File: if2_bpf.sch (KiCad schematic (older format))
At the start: 12 parts

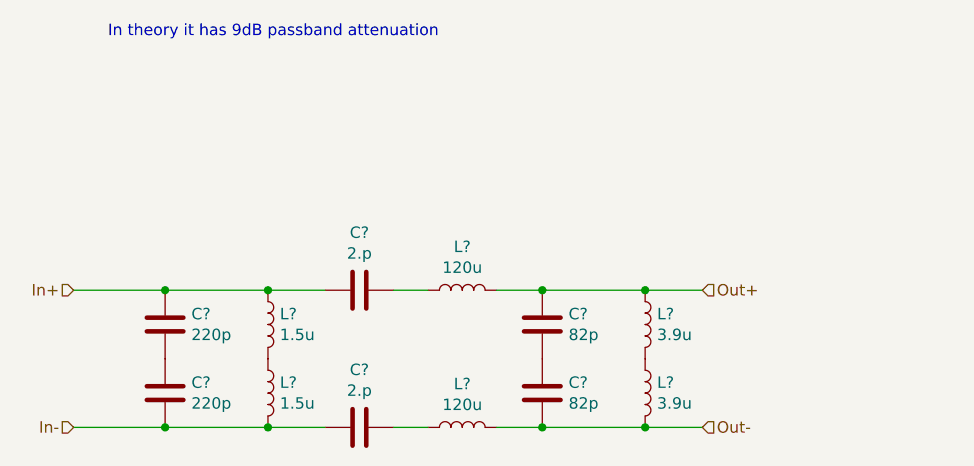
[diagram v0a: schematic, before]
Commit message: If2 50 ohm filter
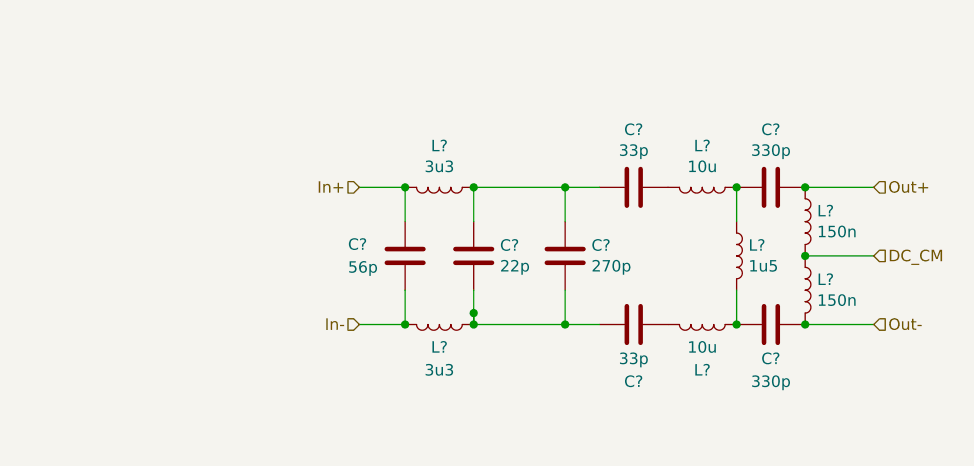
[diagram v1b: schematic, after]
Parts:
- removed C? (x2): 220p, symbol Device:C
- removed C? (x2): 2.p, symbol Device:C
- removed C? (x2): 82p, symbol Device:C
- removed L? (x2): 1.5u, symbol Device:L
- removed L? (x2): 120u, symbol Device:L
- removed L? (x2): 3.9u, symbol Device:L
- added C?: 56p, symbol Device:C
- added C?: 22p, symbol Device:C
- added C? (x2): 33p, symbol Device:C
- added C? (x2): 330p, symbol Device:C
- added C?: 270p, symbol Device:C
- added L? (x2): 3u3, symbol Device:L
- added L? (x2): 10u, symbol Device:L
- added L?: 1u5, symbol Device:L
- added L? (x2): 150n, symbol Device:L
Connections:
- net In+: now also C?.1, L?.2
- net In-: now also C?.2, L?.2
- net Out+: now also C?.1, L?.1
- net Out-: now also C?.2, L?.2
- new net: C?.1, C?.1, C?.2, L?.1
- new net: C?.2, C?.2, C?.2, L?.1
- new net: C?.1, L?.2 (x2)
- new net: C?.2, L?.1, L?.1
- new net: C?.1, L?.1, L?.2
- new net DC_CM: L?.1, L?.2
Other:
- note removed: "In theory it has 9dB passband attenuation\n"

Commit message: Initalize receiver test circuit
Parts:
- gave numbers to parts that had none: 14
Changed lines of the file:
@@
 $Descr A4 11693 8268
 encoding utf-8
-Sheet 5 9
+Sheet 5 7
 Title ""
 Date ""
@@
 In-
 $Comp
-L Device:C C?
+L Device:C C24
 U 1 1 5FECCD6C
 P 4750 2300
-F 0 "C?" H 4500 2350 50  0000 L CNN
+F 0 "C24" H 4500 2350 50  0000 L CNN
 F 1 "56p" H 4500 2250 50  0000 L CNN
 F 2 "" H 4788 2150 50  0001 C CNN
@@
 $EndComp
 $Comp
-L Device:L L?
+L Device:L L11
 U 1 1 5FECD51B
 P 4900 2000
-F 0 "L?" V 4719 2000 50  0000 C CNN
+F 0 "L11" V 4719 2000 50  0000 C CNN
 F 1 "3u3" V 4810 2000 50  0000 C CNN
 F 2 "" H 4900 2000 50  0001 C CNN
@@
 $EndComp
 $Comp
-L Device:L L?
+L Device:L L12
 U 1 1 5FECDA86
 P 4900 2600
-F 0 "L?" V 5000 2600 50  0000 C CNN
+F 0 "L12" V 5000 2600 50  0000 C CNN
 F 1 "3u3" V 5100 2600 50  0000 C CNN
 F 2 "" H 4900 2600 50  0001 C CNN
@@
 $EndComp
 $Comp
-L Device:C C?
+L Device:C C25
 U 1 1 5FECE707
 P 5050 2300
-F 0 "C?" H 5165 2346 50  0000 L CNN
+F 0 "C25" H 5165 2346 50  0000 L CNN
 F 1 "22p" H 5165 2255 50  0000 L CNN
 F 2 "" H 5088 2150 50  0001 C CNN
@@
 $EndComp
 $Comp
-L Device:C C?
+L Device:C C27
 U 1 1 5FECF0CE
 P 5750 2000
-F 0 "C?" V 5498 2000 50  0000 C CNN
+F 0 "C27" V 5498 2000 50  0000 C CNN
 F 1 "33p" V 5589 2000 50  0000 C CNN
 F 2 "" H 5788 1850 50  0001 C CNN
@@
 $EndComp
 $Comp
-L Device:L L?
+L Device:L L13
 U 1 1 5FECF5C4
 P 6050 2000
-F 0 "L?" V 5869 2000 50  0000 C CNN
+F 0 "L13" V 5869 2000 50  0000 C CNN
 F 1 "10u" V 5960 2000 50  0000 C CNN
 F 2 "" H 6050 2000 50  0001 C CNN
@@
 $EndComp
 $Comp
-L Device:L L?
+L Device:L L15
 U 1 1 5FED0166
 P 6200 2300
-F 0 "L?" H 6252 2346 50  0000 L CNN
+F 0 "L15" H 6252 2346 50  0000 L CNN
 F 1 "1u5" H 6252 2255 50  0000 L CNN
 F 2 "" H 6200 2300 50  0001 C CNN
@@
 $EndComp
 $Comp
-L Device:C C?
+L Device:C C29
 U 1 1 5FED1E6D
 P 6350 2000
-F 0 "C?" V 6098 2000 50  0000 C CNN
+F 0 "C29" V 6098 2000 50  0000 C CNN
 F 1 "330p" V 6189 2000 50  0000 C CNN
 F 2 "" H 6388 1850 50  0001 C CNN
@@
 $EndComp
 $Comp
-L Device:L L?
+L Device:L L16
 U 1 1 5FED258A
 P 6500 2150
-F 0 "L?" H 6552 2196 50  0000 L CNN
+F 0 "L16" H 6552 2196 50  0000 L CNN
 F 1 "150n" H 6552 2105 50  0000 L CNN
 F 2 "" H 6500 2150 50  0001 C CNN
@@
 $EndComp
 $Comp
-L Device:L L?
+L Device:L L17
 U 1 1 5FED3759
 P 6500 2450
-F 0 "L?" H 6552 2496 50  0000 L CNN
+F 0 "L17" H 6552 2496 50  0000 L CNN
 F 1 "150n" H 6552 2405 50  0000 L CNN
 F 2 "" H 6500 2450 50  0001 C CNN
@@
 DC_CM
 $Comp
-L Device:C C?
+L Device:C C30
 U 1 1 5FED6CF7
 P 6350 2600
-F 0 "C?" V 6200 2600 50  0000 C CNN
+F 0 "C30" V 6200 2600 50  0000 C CNN
 F 1 "330p" V 6100 2600 50  0000 C CNN
 F 2 "" H 6388 2450 50  0001 C CNN
@@
 Connection ~ 6500 2600
 $Comp
-L Device:L L?
+L Device:L L14
 U 1 1 5FED7875
 P 6050 2600
-F 0 "L?" V 6250 2600 50  0000 C CNN
+F 0 "L14" V 6250 2600 50  0000 C CNN
 F 1 "10u" V 6150 2600 50  0000 C CNN
 F 2 "" H 6050 2600 50  0001 C CNN
@@
 $EndComp
 $Comp
-L Device:C C?
+L Device:C C28
 U 1 1 5FED7DBE
 P 5750 2600
-F 0 "C?" V 6000 2600 50  0000 C CNN
+F 0 "C28" V 6000 2600 50  0000 C CNN
 F 1 "33p" V 5900 2600 50  0000 C CNN
 F 2 "" H 5788 2450 50  0001 C CNN
@@
 Connection ~ 6200 2600
 $Comp
-L Device:C C?
+L Device:C C26
 U 1 1 5FEE51AD
 P 5450 2300
-F 0 "C?" H 5565 2346 50  0000 L CNN
+F 0 "C26" H 5565 2346 50  0000 L CNN
 F 1 "270p" H 5565 2255 50  0000 L CNN
 F 2 "" H 5488 2150 50  0001 C CNN

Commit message: Nyáktervezésre majdnem kész
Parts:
- C24, C25, C26, C27, C28, C29, C30: footprint (none) -> Capacitor_SMD:C_0805_2012Metric_Pad1.15x1.40mm_HandSolder
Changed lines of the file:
@@
 F 0 "C24" H 4500 2350 50  0000 L CNN
 F 1 "56p" H 4500 2250 50  0000 L CNN
-F 2 "" H 4788 2150 50  0001 C CNN
+F 2 "Capacitor_SMD:C_0805_2012Metric_Pad1.15x1.40mm_HandSolder" H 4788 2150 50  0001 C CNN
 F 3 "~" H 4750 2300 50  0001 C CNN
 	1    4750 2300
@@
 F 0 "C25" H 5165 2346 50  0000 L CNN
 F 1 "22p" H 5165 2255 50  0000 L CNN
-F 2 "" H 5088 2150 50  0001 C CNN
+F 2 "Capacitor_SMD:C_0805_2012Metric_Pad1.15x1.40mm_HandSolder" H 5088 2150 50  0001 C CNN
 F 3 "~" H 5050 2300 50  0001 C CNN
 	1    5050 2300
@@
 F 0 "C27" V 5498 2000 50  0000 C CNN
 F 1 "33p" V 5589 2000 50  0000 C CNN
-F 2 "" H 5788 1850 50  0001 C CNN
+F 2 "Capacitor_SMD:C_0805_2012Metric_Pad1.15x1.40mm_HandSolder" H 5788 1850 50  0001 C CNN
 F 3 "~" H 5750 2000 50  0001 C CNN
 	1    5750 2000
@@
 F 0 "C29" V 6098 2000 50  0000 C CNN
 F 1 "330p" V 6189 2000 50  0000 C CNN
-F 2 "" H 6388 1850 50  0001 C CNN
+F 2 "Capacitor_SMD:C_0805_2012Metric_Pad1.15x1.40mm_HandSolder" H 6388 1850 50  0001 C CNN
 F 3 "~" H 6350 2000 50  0001 C CNN
 	1    6350 2000
@@
 F 0 "C30" V 6200 2600 50  0000 C CNN
 F 1 "330p" V 6100 2600 50  0000 C CNN
-F 2 "" H 6388 2450 50  0001 C CNN
+F 2 "Capacitor_SMD:C_0805_2012Metric_Pad1.15x1.40mm_HandSolder" H 6388 2450 50  0001 C CNN
 F 3 "~" H 6350 2600 50  0001 C CNN
 	1    6350 2600
@@
 F 0 "C28" V 6000 2600 50  0000 C CNN
 F 1 "33p" V 5900 2600 50  0000 C CNN
-F 2 "" H 5788 2450 50  0001 C CNN
+F 2 "Capacitor_SMD:C_0805_2012Metric_Pad1.15x1.40mm_HandSolder" H 5788 2450 50  0001 C CNN
 F 3 "~" H 5750 2600 50  0001 C CNN
 	1    5750 2600
@@
 F 0 "C26" H 5565 2346 50  0000 L CNN
 F 1 "270p" H 5565 2255 50  0000 L CNN
-F 2 "" H 5488 2150 50  0001 C CNN
+F 2 "Capacitor_SMD:C_0805_2012Metric_Pad1.15x1.40mm_HandSolder" H 5488 2150 50  0001 C CNN
 F 3 "~" H 5450 2300 50  0001 C CNN
 	1    5450 2300
@@
 Wire Wire Line
 	5450 2000 5050 2000
-Connection ~ 5050 2550
 Wire Wire Line
 	5050 2550 5050 2600

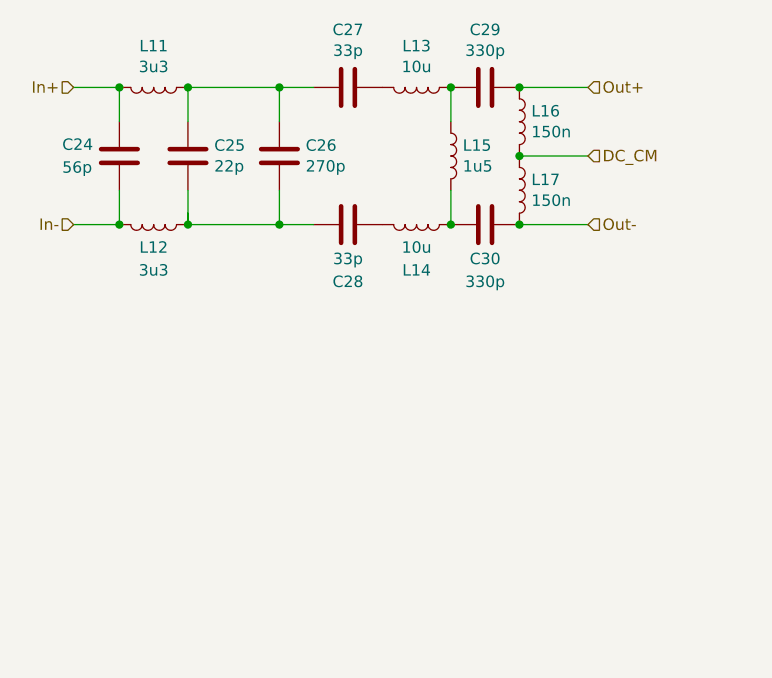
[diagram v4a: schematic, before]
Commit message: Receiver test panel ++
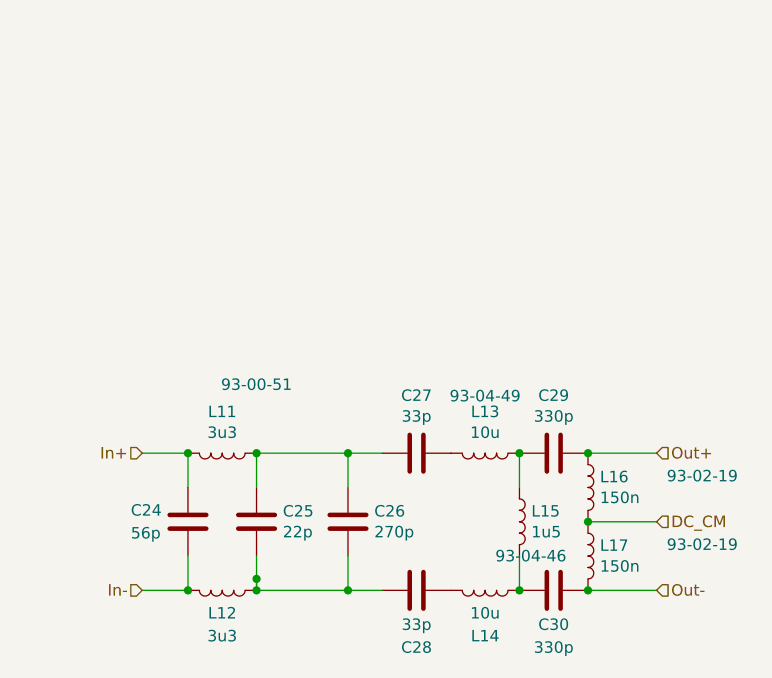
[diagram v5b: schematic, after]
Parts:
- L11: footprint (none) -> Inductor_SMD:L_1210_3225Metric_Pad1.42x2.65mm_HandSolder; Lomex (none) -> 93-00-51
- L12, L14: footprint (none) -> Inductor_SMD:L_1210_3225Metric_Pad1.42x2.65mm_HandSolder
- L13: footprint (none) -> Inductor_SMD:L_1210_3225Metric_Pad1.42x2.65mm_HandSolder; Lomex (none) -> 93-04-49
- L15: footprint (none) -> Inductor_SMD:L_1210_3225Metric_Pad1.42x2.65mm_HandSolder; Lomex (none) -> 93-04-46
- L16, L17: footprint (none) -> Inductor_SMD:L_1210_3225Metric_Pad1.42x2.65mm_HandSolder; Lomex (none) -> 93-02-19
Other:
- moved on the sheet: C24, C25, C26, C27, C28, C29, C30, L11, L12, L13, L14, L15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

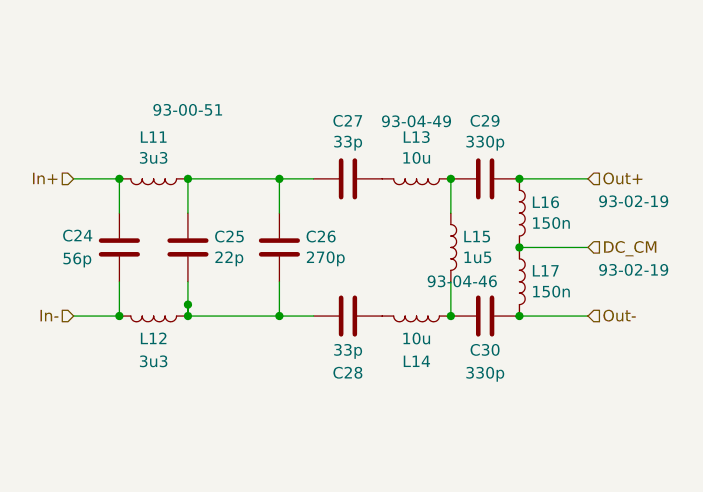
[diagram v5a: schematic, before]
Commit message: IF2 filter and amp recalculate
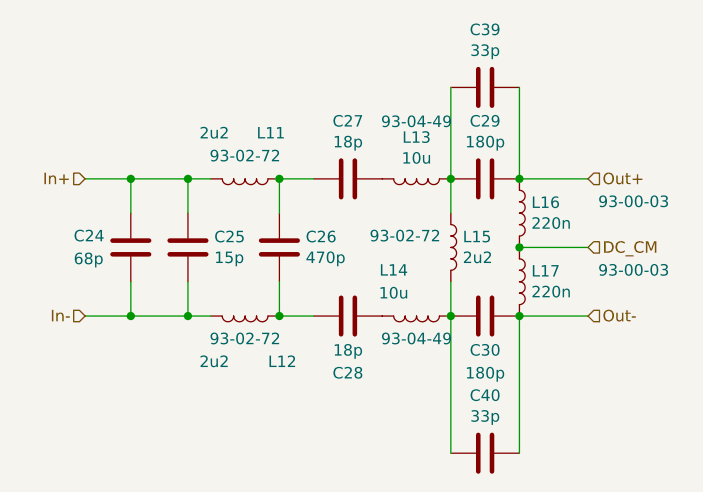
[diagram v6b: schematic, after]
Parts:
- added C39, C40: 33p, Capacitor_SMD:C_0805_2012Metric_Pad1.15x1.40mm_HandSolder, symbol Device:C
- C24: value 56p -> 68p
- C25: value 22p -> 15p
- C26: value 270p -> 470p
- C27, C28: value 33p -> 18p
- C29, C30: value 330p -> 180p
- L11: value 3u3 -> 2u2; footprint Inductor_SMD:L_1210_3225Metric_Pad1.42x2.65mm_HandSolder -> Inductor_SMD:L_0805_2012Metric_Pad1.15x1.40mm_HandSolder; Lomex 93-00-51 -> 93-02-72
- L12: value 3u3 -> 2u2; footprint Inductor_SMD:L_1210_3225Metric_Pad1.42x2.65mm_HandSolder -> Inductor_SMD:L_0805_2012Metric_Pad1.15x1.40mm_HandSolder; Lomex (none) -> 93-02-72
- L14: Lomex (none) -> 93-04-49
- L15: value 1u5 -> 2u2; footprint Inductor_SMD:L_1210_3225Metric_Pad1.42x2.65mm_HandSolder -> Inductor_SMD:L_0805_2012Metric_Pad1.15x1.40mm_HandSolder; Lomex 93-04-46 -> 93-02-72
- L16, L17: value 150n -> 220n; Lomex 93-02-19 -> 93-00-03
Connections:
- net In+: now also C25.1
- net In-: now also C25.2
- net Out+: now also C39.1
- net Out-: now also C40.1
- net at C26.1, C27.2, L11.1: no longer C25.1
- net at C26.2, C28.2, L12.1: no longer C25.2
- net at C29.2, L13.1, L15.1: now also C39.2
- net at C30.1, L14.1, L15.2: now also C40.2
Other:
- moved on the sheet: C24
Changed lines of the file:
@@
 Text HLabel 7100 4200 2    50   Input ~ 0
 Out-
-Text HLabel 4850 3600 0    50   Input ~ 0
+Text HLabel 4900 3600 0    50   Input ~ 0
 In+
-Text HLabel 4850 4200 0    50   Input ~ 0
+Text HLabel 4900 4200 0    50   Input ~ 0
 In-
 $Comp
 L Device:C C24
 U 1 1 5FECCD6C
-P 5050 3900
-F 0 "C24" H 4800 3950 50  0000 L CNN
-F 1 "56p" H 4800 3850 50  0000 L CNN
-F 2 "Capacitor_SMD:C_0805_2012Metric_Pad1.15x1.40mm_HandSolder" H 5088 3750 50  0001 C CNN
-F 3 "~" H 5050 3900 50  0001 C CNN
-	1    5050 3900
-	1    0    0    -1
-$EndComp
-$Comp
-L Device:L L11
-U 1 1 5FECD51B
-P 5200 3600
-F 0 "L11" V 5019 3600 50  0000 C CNN
-F 1 "3u3" V 5110 3600 50  0000 C CNN
-F 2 "Inductor_SMD:L_1210_3225Metric_Pad1.42x2.65mm_HandSolder" H 5200 3600 50  0001 C CNN
-F 3 "~" H 5200 3600 50  0001 C CNN
-F 4 "93-00-51" V 4900 3750 50  0000 C CNN "Lomex"
-	1    5200 3600
-	0    1    1    0
-$EndComp
-$Comp
-L Device:L L12
-U 1 1 5FECDA86
-P 5200 4200
-F 0 "L12" V 5300 4200 50  0000 C CNN
-F 1 "3u3" V 5400 4200 50  0000 C CNN
-F 2 "Inductor_SMD:L_1210_3225Metric_Pad1.42x2.65mm_HandSolder" H 5200 4200 50  0001 C CNN
-F 3 "~" H 5200 4200 50  0001 C CNN
-	1    5200 4200
-	0    1    1    0
+P 5100 3900
+F 0 "C24" H 4850 3950 50  0000 L CNN
+F 1 "68p" H 4850 3850 50  0000 L CNN
+F 2 "Capacitor_SMD:C_0805_2012Metric_Pad1.15x1.40mm_HandSolder" H 5138 3750 50  0001 C CNN
+F 3 "~" H 5100 3900 50  0001 C CNN
+	1    5100 3900
+	1    0    0    -1
 $EndComp
 $Comp
@@
 P 5350 3900
 F 0 "C25" H 5465 3946 50  0000 L CNN
-F 1 "22p" H 5465 3855 50  0000 L CNN
+F 1 "15p" H 5465 3855 50  0000 L CNN
 F 2 "Capacitor_SMD:C_0805_2012Metric_Pad1.15x1.40mm_HandSolder" H 5388 3750 50  0001 C CNN
 F 3 "~" H 5350 3900 50  0001 C CNN
@@
 P 6050 3600
 F 0 "C27" V 5798 3600 50  0000 C CNN
-F 1 "33p" V 5889 3600 50  0000 C CNN
+F 1 "18p" V 5889 3600 50  0000 C CNN
 F 2 "Capacitor_SMD:C_0805_2012Metric_Pad1.15x1.40mm_HandSolder" H 6088 3450 50  0001 C CNN
 F 3 "~" H 6050 3600 50  0001 C CNN
@@
 P 6500 3900
 F 0 "L15" H 6552 3946 50  0000 L CNN
-F 1 "1u5" H 6552 3855 50  0000 L CNN
-F 2 "Inductor_SMD:L_1210_3225Metric_Pad1.42x2.65mm_HandSolder" H 6500 3900 50  0001 C CNN
+F 1 "2u2" H 6552 3855 50  0000 L CNN
+F 2 "Inductor_SMD:L_0805_2012Metric_Pad1.15x1.40mm_HandSolder" H 6500 3900 50  0001 C CNN
 F 3 "~" H 6500 3900 50  0001 C CNN
-F 4 "93-04-46" H 6550 3750 50  0000 C CNN "Lomex"
+F 4 "93-02-72" H 6300 3950 50  0000 C CNN "Lomex"
 	1    6500 3900
 	1    0    0    -1
@@
 P 6650 3600
 F 0 "C29" V 6398 3600 50  0000 C CNN
-F 1 "330p" V 6489 3600 50  0000 C CNN
+F 1 "180p" V 6489 3600 50  0000 C CNN
 F 2 "Capacitor_SMD:C_0805_2012Metric_Pad1.15x1.40mm_HandSolder" H 6688 3450 50  0001 C CNN
 F 3 "~" H 6650 3600 50  0001 C CNN
@@
 P 6800 3750
 F 0 "L16" H 6852 3796 50  0000 L CNN
-F 1 "150n" H 6852 3705 50  0000 L CNN
+F 1 "220n" H 6852 3705 50  0000 L CNN
 F 2 "Inductor_SMD:L_1210_3225Metric_Pad1.42x2.65mm_HandSolder" H 6800 3750 50  0001 C CNN
 F 3 "~" H 6800 3750 50  0001 C CNN
-F 4 "93-02-19" H 7300 3800 50  0000 C CNN "Lomex"
+F 4 "93-00-03" H 7300 3800 50  0000 C CNN "Lomex"
 	1    6800 3750
 	1    0    0    -1
 $EndComp
-$Comp
-L Device:L L17
-U 1 1 5FED3759
-P 6800 4050
-F 0 "L17" H 6852 4096 50  0000 L CNN
-F 1 "150n" H 6852 4005 50  0000 L CNN
-F 2 "Inductor_SMD:L_1210_3225Metric_Pad1.42x2.65mm_HandSolder" H 6800 4050 50  0001 C CNN
-F 3 "~" H 6800 4050 50  0001 C CNN
-F 4 "93-02-19" H 7300 4100 50  0000 C CNN "Lomex"
-	1    6800 4050
-	1    0    0    -1
-$EndComp
-Wire Wire Line
-	4850 4200 5050 4200
-Wire Wire Line
-	5050 4200 5050 4050
-Connection ~ 5050 4200
-Wire Wire Line
-	5050 3750 5050 3600
-Wire Wire Line
-	5050 3600 4850 3600
-Connection ~ 5050 3600
-Wire Wire Line
-	5350 3750 5350 3600
+Wire Wire Line
+	4900 4200 5100 4200
+Wire Wire Line
+	5100 4200 5100 4050
+Wire Wire Line
+	5100 3750 5100 3600
+Wire Wire Line
+	5100 3600 4900 3600
 Wire Wire Line
 	6500 3750 6500 3600
@@
 Wire Wire Line
 	6800 3900 7100 3900
-Connection ~ 6800 3900
 Text HLabel 7100 3900 2    50   Input ~ 0
 DC_CM
@@
 P 6650 4200
 F 0 "C30" V 6500 4200 50  0000 C CNN
-F 1 "330p" V 6400 4200 50  0000 C CNN
+F 1 "180p" V 6400 4200 50  0000 C CNN
 F 2 "Capacitor_SMD:C_0805_2012Metric_Pad1.15x1.40mm_HandSolder" H 6688 4050 50  0001 C CNN
 F 3 "~" H 6650 4200 50  0001 C CNN
@@
 	0    -1   -1   0
 $EndComp
-Connection ~ 6800 4200
-$Comp
-L Device:L L14
-U 1 1 5FED7875
-P 6350 4200
-F 0 "L14" V 6550 4200 50  0000 C CNN
-F 1 "10u" V 6450 4200 50  0000 C CNN
-F 2 "Inductor_SMD:L_1210_3225Metric_Pad1.42x2.65mm_HandSolder" H 6350 4200 50  0001 C CNN
-F 3 "~" H 6350 4200 50  0001 C CNN
-	1    6350 4200
-	0    1    1    0
-$EndComp
 $Comp
 L Device:C C28
@@
 P 6050 4200
 F 0 "C28" V 6300 4200 50  0000 C CNN
-F 1 "33p" V 6200 4200 50  0000 C CNN
+F 1 "18p" V 6200 4200 50  0000 C CNN
 F 2 "Capacitor_SMD:C_0805_2012Metric_Pad1.15x1.40mm_HandSolder" H 6088 4050 50  0001 C CNN
 F 3 "~" H 6050 4200 50  0001 C CNN
@@
 Wire Wire Line
 	6500 4050 6500 4200
-Connection ~ 6500 4200
 $Comp
 L Device:C C26
@@
 P 5750 3900
 F 0 "C26" H 5865 3946 50  0000 L CNN
-F 1 "270p" H 5865 3855 50  0000 L CNN
+F 1 "470p" H 5865 3855 50  0000 L CNN
 F 2 "Capacitor_SMD:C_0805_2012Metric_Pad1.15x1.40mm_HandSolder" H 5788 3750 50  0001 C CNN
 F 3 "~" H 5750 3900 50  0001 C CNN
@@
 Wire Wire Line
 	5900 4200 5750 4200
+Wire Wire Line
+	5750 4050 5750 4200
+Wire Wire Line
+	5900 3600 5750 3600
+Wire Wire Line
+	5750 3750 5750 3600
+Wire Wire Line
+	5450 3600 5350 3600
+Connection ~ 5100 3600
+Wire Wire Line
+	5350 3750 5350 3600
+Connection ~ 5350 3600
+Wire Wire Line
+	5350 3600 5100 3600
+Wire Wire Line
+	5450 4200 5350 4200
+Connection ~ 5100 4200
+Wire Wire Line
+	5350 4050 5350 4200
 Connection ~ 5350 4200
 Wire Wire Line
-	5750 4050 5750 4200
+	5350 4200 5100 4200
+$Comp
+L Device:L L11
+U 1 1 60028C2F
+P 5600 3600
+F 0 "L11" V 5400 3650 50  0000 L CNN
+F 1 "2u2" V 5400 3400 50  0000 L CNN
+F 2 "Inductor_SMD:L_0805_2012Metric_Pad1.15x1.40mm_HandSolder" H 5600 3600 50  0001 C CNN
+F 3 "~" H 5600 3600 50  0001 C CNN
+F 4 "93-02-72" V 5500 3600 50  0000 C CNN "Lomex"
+	1    5600 3600
+	0    1    1    0
+$EndComp
+Connection ~ 5750 3600
+$Comp
+L Device:L L12
+U 1 1 6002A199
+P 5600 4200
+F 0 "L12" V 5800 4300 50  0000 L CNN
+F 1 "2u2" V 5800 4000 50  0000 L CNN
+F 2 "Inductor_SMD:L_0805_2012Metric_Pad1.15x1.40mm_HandSolder" H 5600 4200 50  0001 C CNN
+F 3 "~" H 5600 4200 50  0001 C CNN
+F 4 "93-02-72" V 5700 4200 50  0000 C CNN "Lomex"
+	1    5600 4200
+	0    1    1    0
+$EndComp
 Connection ~ 5750 4200
-Wire Wire Line
-	5750 4200 5350 4200
-Wire Wire Line
-	5900 3600 5750 3600
-Connection ~ 5350 3600
-Wire Wire Line
-	5750 3750 5750 3600
-Connection ~ 5750 3600
-Wire Wire Line
-	5750 3600 5350 3600
-Connection ~ 5350 4150
-Wire Wire Line
-	5350 4150 5350 4200
-Wire Wire Line
-	5350 4050 5350 4200
+$Comp
+L Device:L L14
+U 1 1 6002AC30
+P 6350 4200
+F 0 "L14" V 6150 4100 50  0000 C CNN
+F 1 "10u" V 6250 4100 50  0000 C CNN
+F 2 "Inductor_SMD:L_1210_3225Metric_Pad1.42x2.65mm_HandSolder" H 6350 4200 50  0001 C CNN
+F 3 "~" H 6350 4200 50  0001 C CNN
+F 4 "93-04-49" V 6450 4200 50  0000 C CNN "Lomex"
+	1    6350 4200
+	0    1    1    0
+$EndComp
+Connection ~ 6500 4200
+$Comp
+L Device:L L17
+U 1 1 6002B609
+P 6800 4050
+F 0 "L17" H 6852 4096 50  0000 L CNN
+F 1 "220n" H 6852 4005 50  0000 L CNN
+F 2 "Inductor_SMD:L_1210_3225Metric_Pad1.42x2.65mm_HandSolder" H 6800 4050 50  0001 C CNN
+F 3 "~" H 6800 4050 50  0001 C CNN
+F 4 "93-00-03" H 7300 4100 50  0000 C CNN "Lomex"
+	1    6800 4050
+	1    0    0    -1
+$EndComp
+Connection ~ 6800 3900
+Connection ~ 6800 4200
+Wire Wire Line
+	6500 3200 6500 3600
+Wire Wire Line
+	6800 3200 6800 3600
+$Comp
+L Device:C C39
+U 1 1 6002CCED
+P 6650 3200
+F 0 "C39" V 6398 3200 50  0000 C CNN
+F 1 "33p" V 6489 3200 50  0000 C CNN
+F 2 "Capacitor_SMD:C_0805_2012Metric_Pad1.15x1.40mm_HandSolder" H 6688 3050 50  0001 C CNN
+F 3 "~" H 6650 3200 50  0001 C CNN
+	1    6650 3200
+	0    1    1    0
+$EndComp
+$Comp
+L Device:C C40
+U 1 1 6002D1C8
+P 6650 4800
+F 0 "C40" V 6398 4800 50  0000 C CNN
+F 1 "33p" V 6489 4800 50  0000 C CNN
+F 2 "Capacitor_SMD:C_0805_2012Metric_Pad1.15x1.40mm_HandSolder" H 6688 4650 50  0001 C CNN
+F 3 "~" H 6650 4800 50  0001 C CNN
+	1    6650 4800
+	0    1    1    0
+$EndComp
+Wire Wire Line
+	6800 4200 6800 4800
+Wire Wire Line
+	6500 4800 6500 4200
 $EndSCHEMATC
